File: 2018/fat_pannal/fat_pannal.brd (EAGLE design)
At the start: 160 x 130.5 mm, 31 parts, among them IC1 MEGA8-P, Q2 BUZ11BV, Q3 BUZ11BV, Q4 BUZ11BV, Q5 BUZ11BV, U1 TSR_1-2450

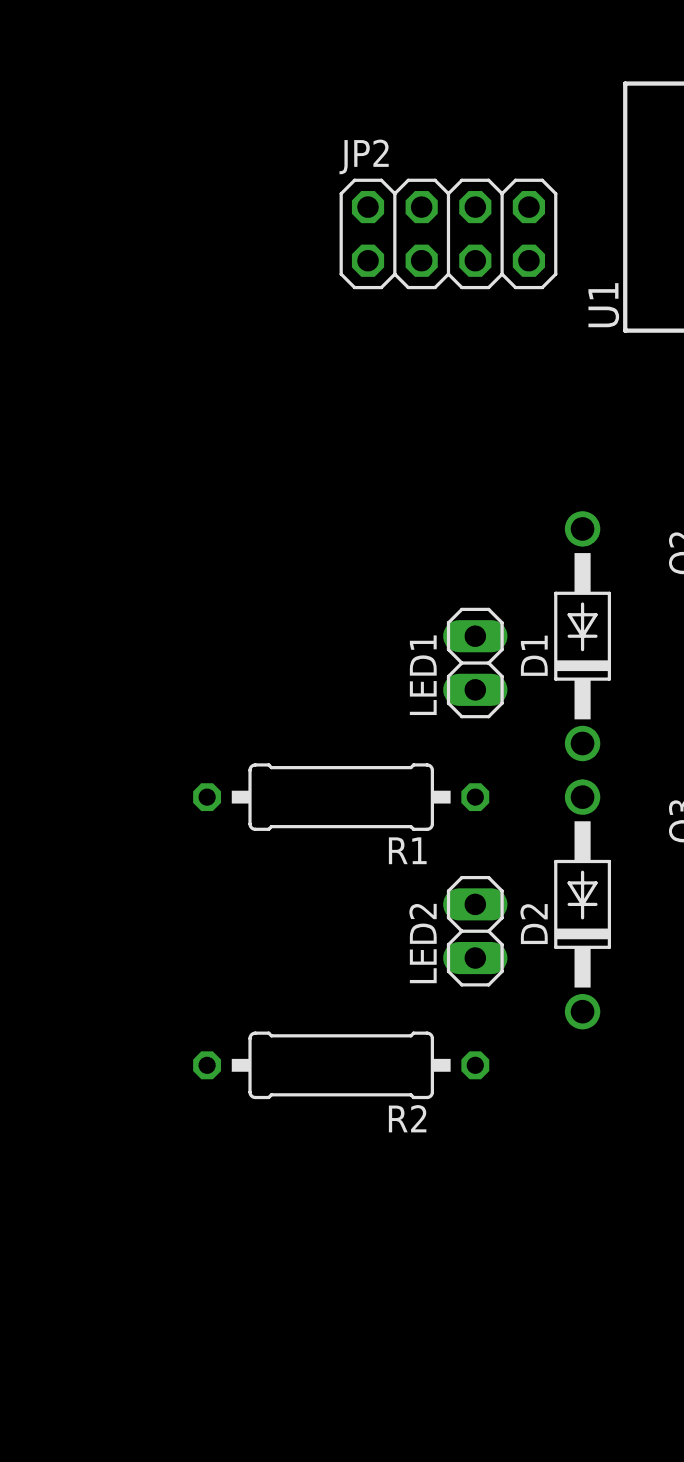
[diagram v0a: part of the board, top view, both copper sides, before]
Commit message: [FAT pannal] Split cavalier in two.
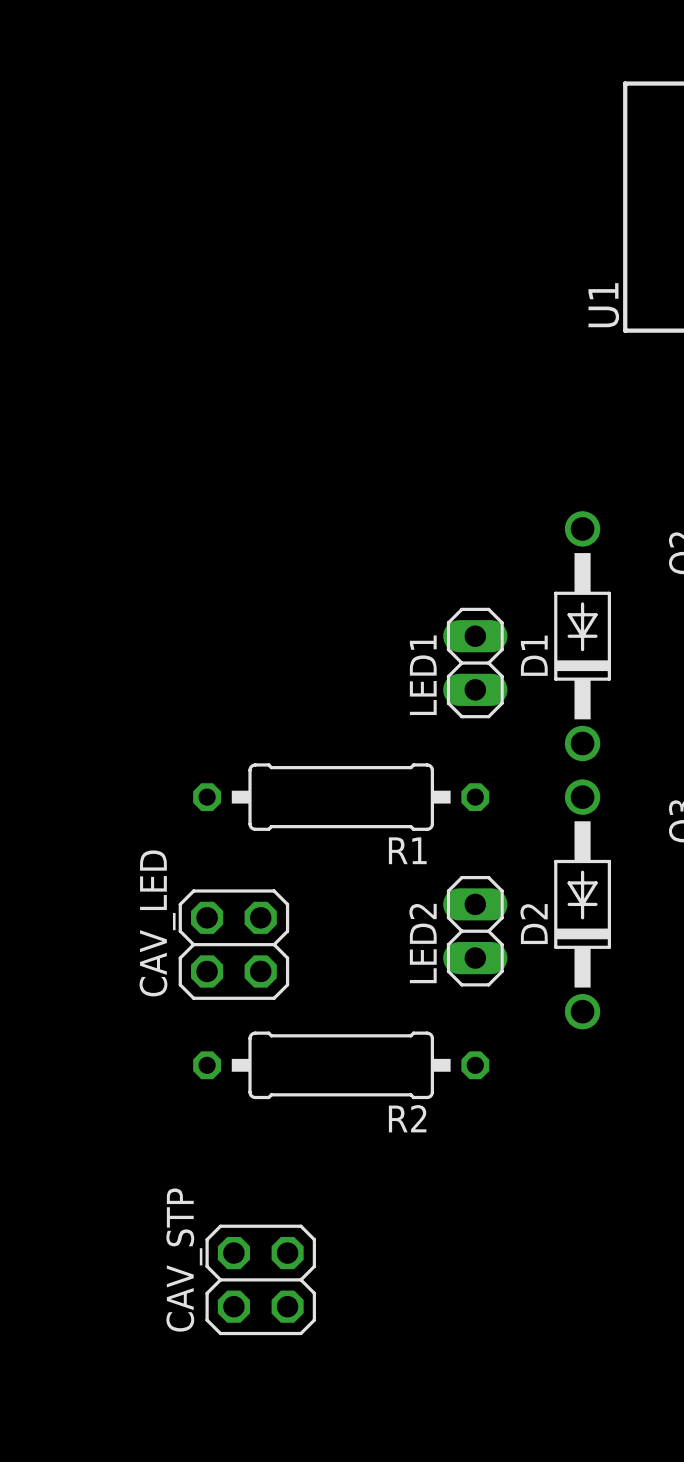
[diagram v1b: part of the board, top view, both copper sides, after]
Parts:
- removed JP2: (no value), pinhead:2X04
- added CAV_LED, CAV_STP: (no value), pinhead:2X02
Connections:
- net GND: now also CAV_LED.1, CAV_LED.3, CAV_STP.1, CAV_STP.3; no longer JP2.1, JP2.3, JP2.5, JP2.7
- net VBAT: now also CAV_LED.2, CAV_STP.2; no longer JP2.4, JP2.6
- net VLED: now also CAV_LED.4; no longer JP2.8
- net VMOT: now also CAV_STP.4; no longer JP2.2
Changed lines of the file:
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@@
 <element name="SERVO3" library="pinhead" package="1X03" value="" x="91.44" y="58.42" rot="R180"/>
 <element name="REGU_5V_POWER" library="diy-modules" package="DC-DC-STEP-DOWN-LM2596" value="DC-DC-STEP-DOWN-LM2596" x="73.66" y="85.09"/>
-<element name="JP2" library="pinhead" package="2X04" value="" x="34.29" y="57.15"/>
 <element name="I2C" library="pinhead" package="1X04" value="" x="101.6" y="62.23" rot="R90"/>
 <element name="UART" library="pinhead" package="1X04" value="" x="60.96" y="59.69" rot="R90"/>
@@
 </element>
 <element name="U1" library="_traco_tsr-1" package="TSR-1" value="TSR_1-2450" x="48.26" y="58.42" rot="R90"/>
+<element name="CAV_STP" library="pinhead" package="2X02" value="" x="25.4" y="7.62" rot="R90"/>
+<element name="CAV_LED" library="pinhead" package="2X02" value="" x="24.13" y="23.495" rot="R90"/>
 </elements>
 <signals>
@@
 <contactref element="REGU_5V_POWER" pad="OUT-"/>
 <contactref element="X1" pad="2"/>
-<contactref element="JP2" pad="1"/>
-<contactref element="JP2" pad="3"/>
-<contactref element="JP2" pad="5"/>
-<contactref element="JP2" pad="7"/>
 <contactref element="STEPPER_DRIVER" pad="GND2"/>
 <contactref element="UART" pad="2"/>
 <contactref element="I2C" pad="2"/>
 <contactref element="U1" pad="2"/>
+<contactref element="CAV_LED" pad="1"/>
+<contactref element="CAV_LED" pad="3"/>
+<contactref element="CAV_STP" pad="3"/>
+<contactref element="CAV_STP" pad="1"/>
 <wire x1="101.6" y1="60.96" x2="93.472" y2="76.454" width="0" layer="19" extent="1-1"/>
 <wire x1="93.98" y1="58.42" x2="101.6" y2="60.96" width="0" layer="19" extent="1-1"/>
@@
 <wire x1="60.96" y1="58.42" x2="58.42" y2="41.91" width="0" layer="19" extent="1-1"/>
 <wire x1="48.26" y1="58.42" x2="60.96" y2="58.42" width="0" layer="19" extent="1-1"/>
-<wire x1="38.1" y1="55.88" x2="48.26" y2="58.42" width="0" layer="19" extent="1-1"/>
-<wire x1="35.56" y1="55.88" x2="38.1" y2="55.88" width="0" layer="19" extent="1-1"/>
-<wire x1="33.02" y1="55.88" x2="35.56" y2="55.88" width="0" layer="19" extent="1-1"/>
-<wire x1="30.48" y1="55.88" x2="33.02" y2="55.88" width="0" layer="19" extent="1-1"/>
 <wire x1="53.848" y1="76.454" x2="48.26" y2="58.42" width="0" layer="19" extent="1-1"/>
 <wire x1="38.1" y1="81.3308" x2="53.848" y2="76.454" width="0" layer="19" extent="1-1"/>
 <wire x1="66.04" y1="7.62" x2="48.26" y2="22.86" width="0" layer="19" extent="1-1"/>
 <wire x1="81.28" y1="7.62" x2="66.04" y2="7.62" width="0" layer="19" extent="1-1"/>
+<wire x1="25.4" y1="24.765" x2="48.26" y2="35.56" width="0" layer="19" extent="1-1"/>
+<wire x1="25.4" y1="22.225" x2="25.4" y2="24.765" width="0" layer="19" extent="1-1"/>
+<wire x1="26.67" y1="8.89" x2="48.26" y2="22.86" width="0" layer="19" extent="1-1"/>
+<wire x1="26.67" y1="6.35" x2="26.67" y2="8.89" width="0" layer="19" extent="1-1"/>
 </signal>
 <signal name="N$3">
@@
 <contactref element="R3" pad="2"/>
 <contactref element="R4" pad="2"/>
-<contactref element="JP2" pad="8"/>
+<contactref element="CAV_LED" pad="4"/>
 <wire x1="121.92" y1="17.78" x2="121.92" y2="30.48" width="0" layer="19" extent="1-1"/>
-<wire x1="38.1" y1="58.42" x2="121.92" y2="30.48" width="0" layer="19" extent="1-1"/>
-<wire x1="22.86" y1="30.48" x2="38.1" y2="58.42" width="0" layer="19" extent="1-1"/>
+<wire x1="22.86" y1="30.48" x2="121.92" y2="30.48" width="0" layer="19" extent="1-1"/>
+<wire x1="22.86" y1="24.765" x2="22.86" y2="30.48" width="0" layer="19" extent="1-1"/>
 <wire x1="22.86" y1="17.78" x2="22.86" y2="30.48" width="0" layer="19" extent="1-1"/>
 </signal>
@@
 <contactref element="REGU_5V_POWER" pad="IN+"/>
 <contactref element="X1" pad="1"/>
-<contactref element="JP2" pad="4"/>
-<contactref element="JP2" pad="6"/>
 <contactref element="U1" pad="1"/>
+<contactref element="CAV_LED" pad="2"/>
+<contactref element="CAV_STP" pad="2"/>
 <wire x1="38.1" y1="86.3346" x2="53.848" y2="93.726" width="0" layer="19" extent="1-1"/>
-<wire x1="35.56" y1="58.42" x2="38.1" y2="86.3346" width="0" layer="19" extent="1-1"/>
-<wire x1="33.02" y1="58.42" x2="35.56" y2="58.42" width="0" layer="19" extent="1-1"/>
-<wire x1="48.26" y1="55.88" x2="35.56" y2="58.42" width="0" layer="19" extent="1-1"/>
+<wire x1="48.26" y1="55.88" x2="38.1" y2="86.3346" width="0" layer="19" extent="1-1"/>
+<wire x1="22.86" y1="22.225" x2="48.26" y2="55.88" width="0" layer="19" extent="1-1"/>
+<wire x1="24.13" y1="6.35" x2="22.86" y2="22.225" width="0" layer="19" extent="1-1"/>
 </signal>
 <signal name="VMOT">
-<contactref element="JP2" pad="2"/>
 <contactref element="STEPPER_DRIVER" pad="VMOT"/>
-<wire x1="83.82" y1="7.62" x2="30.48" y2="58.42" width="0" layer="19" extent="1-1"/>
+<contactref element="CAV_STP" pad="4"/>
+<wire x1="24.13" y1="8.89" x2="83.82" y2="7.62" width="0" layer="19" extent="1-1"/>
 </signal>
 </signals>

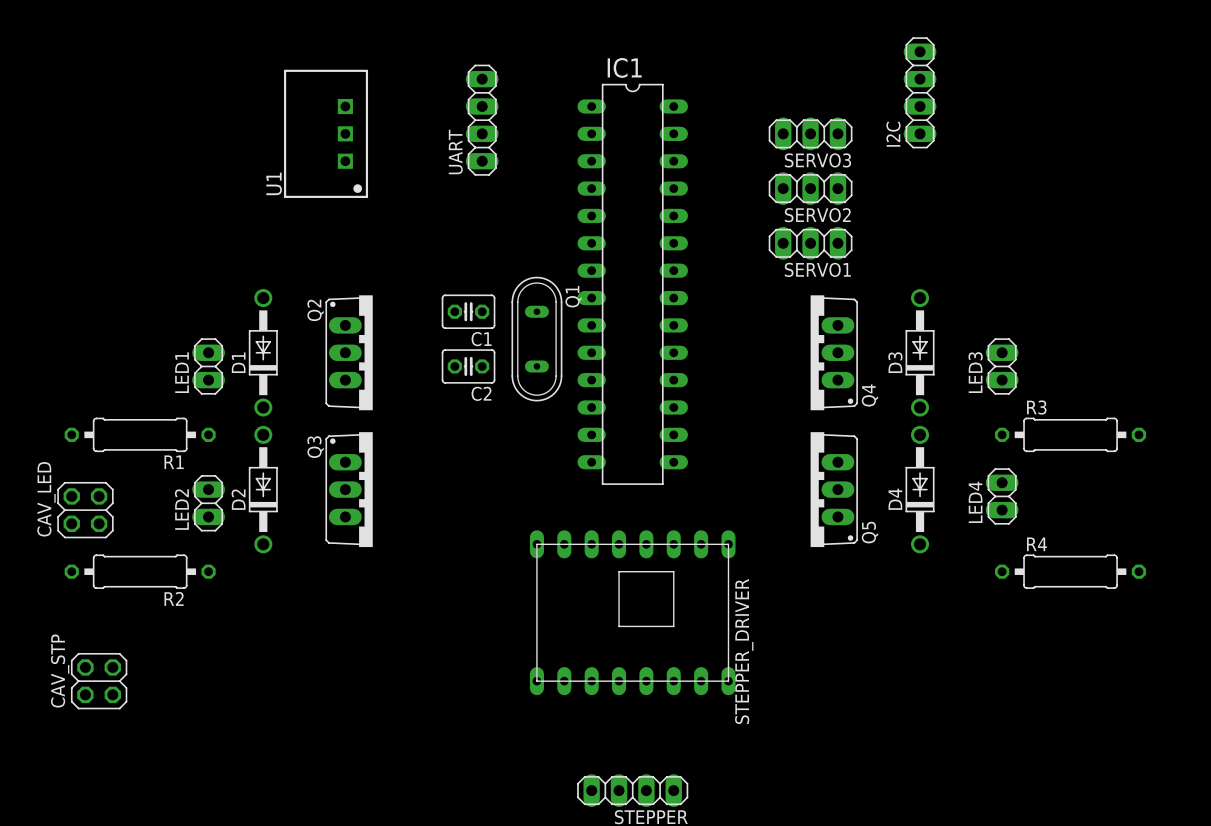
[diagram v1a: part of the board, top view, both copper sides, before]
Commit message: [FAT pannal] Begins routing.
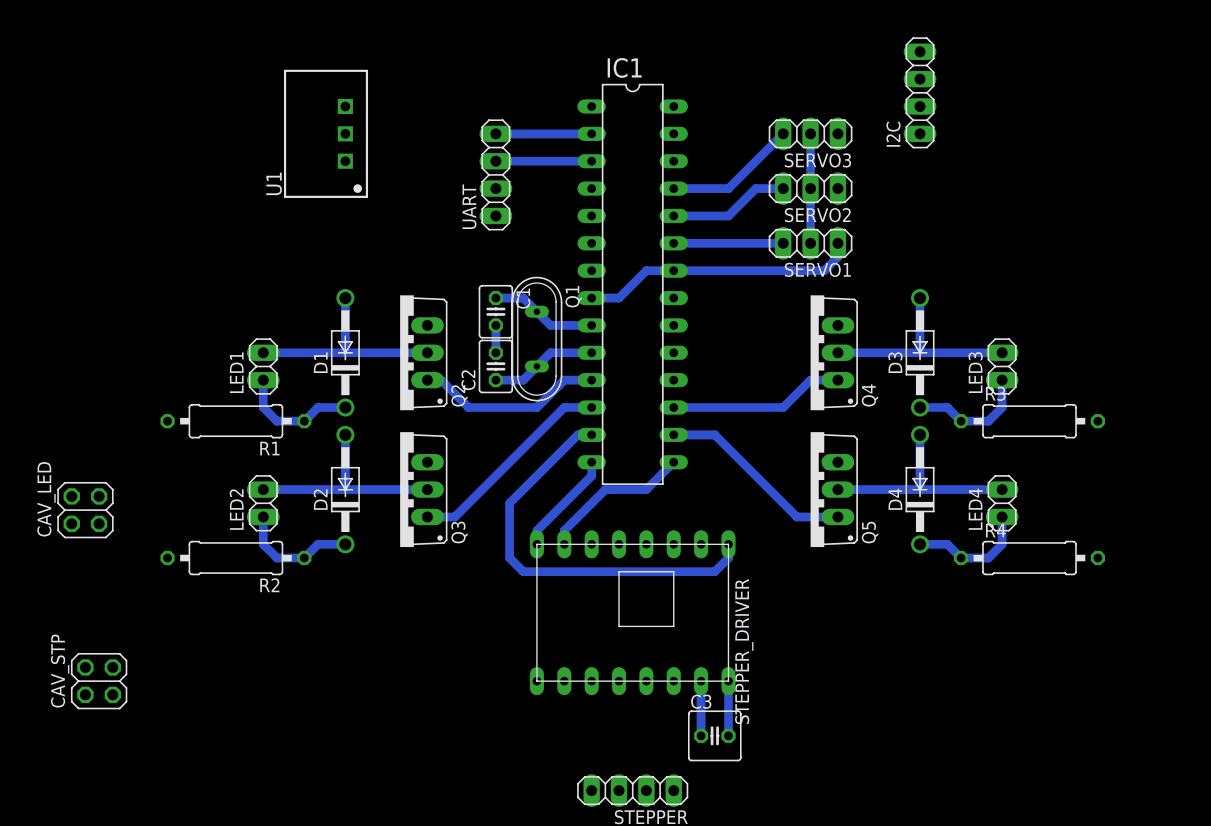
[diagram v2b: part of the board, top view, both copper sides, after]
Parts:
- added C3: 100uF, rcl:C025-050X050
- moved R1 8.98 mm to (38.1, 31.8)
- moved R2 8.98 mm to (38.1, 19.1)
- moved D1 7.62 mm to (48.3, 38.1)
- moved D2 7.62 mm to (48.3, 25.4)
- moved UART 5.24 mm to (62.2, 54.6)
- moved LED1 5.08 mm to (40.6, 36.8)
- moved LED2 5.08 mm to (40.6, 24.1)
- moved R3 4.02 mm to (111.8, 31.8)
- moved R4 4.02 mm to (111.8, 19.1)
- moved Q2 2.54 mm to (53.3, 38.1), turned to 90 degrees
- moved Q3 2.54 mm to (53.3, 25.4), turned to 90 degrees
- moved C1 2.54 mm to (62.2, 41.9), turned to 270 degrees
- moved C2 2.54 mm to (62.2, 36.8), turned to 90 degrees
- moved LED4 0.64 mm to (109.2, 24.1)
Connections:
- net GND: now also C3.1
- net VMOT: now also C3.2
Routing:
- net N$10: track 0.00 -> 38.0 mm
- net GND: track 0.00 -> 33.3 mm
- net N$27: track 0.00 -> 20.3 mm
- net N$26: track 0.00 -> 20.3 mm
- net N$29: track 0.00 -> 20.3 mm
- net N$28: track 0.00 -> 20.3 mm
- net PD6: track 0.00 -> 19.4 mm
- net PB2: track 0.00 -> 18.4 mm
- net PD5: track 0.00 -> 17.3 mm
- net PB3: track 0.00 -> 16.3 mm
- net N$2: track 0.00 -> 14.1 mm
- net SERV3: track 0.00 -> 12.3 mm
- net SERV2: track 0.00 -> 11.2 mm
- net N$23: track 0.00 -> 11.2 mm
- net N$24: track 0.00 -> 11.2 mm
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
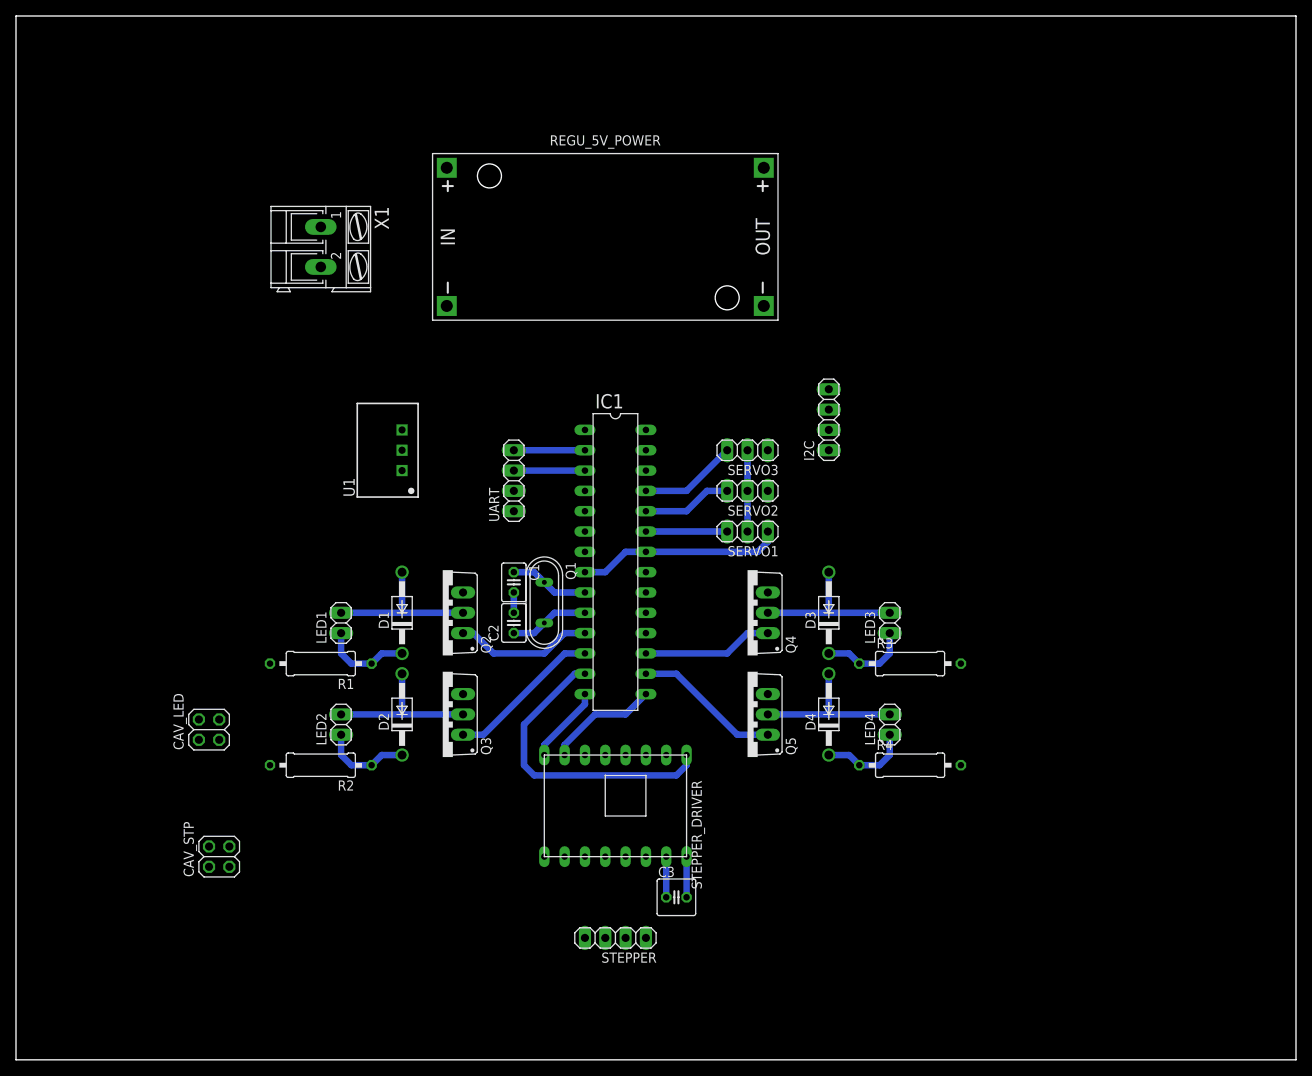
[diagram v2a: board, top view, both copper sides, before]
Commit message: [FAT pannal] Continue routing.
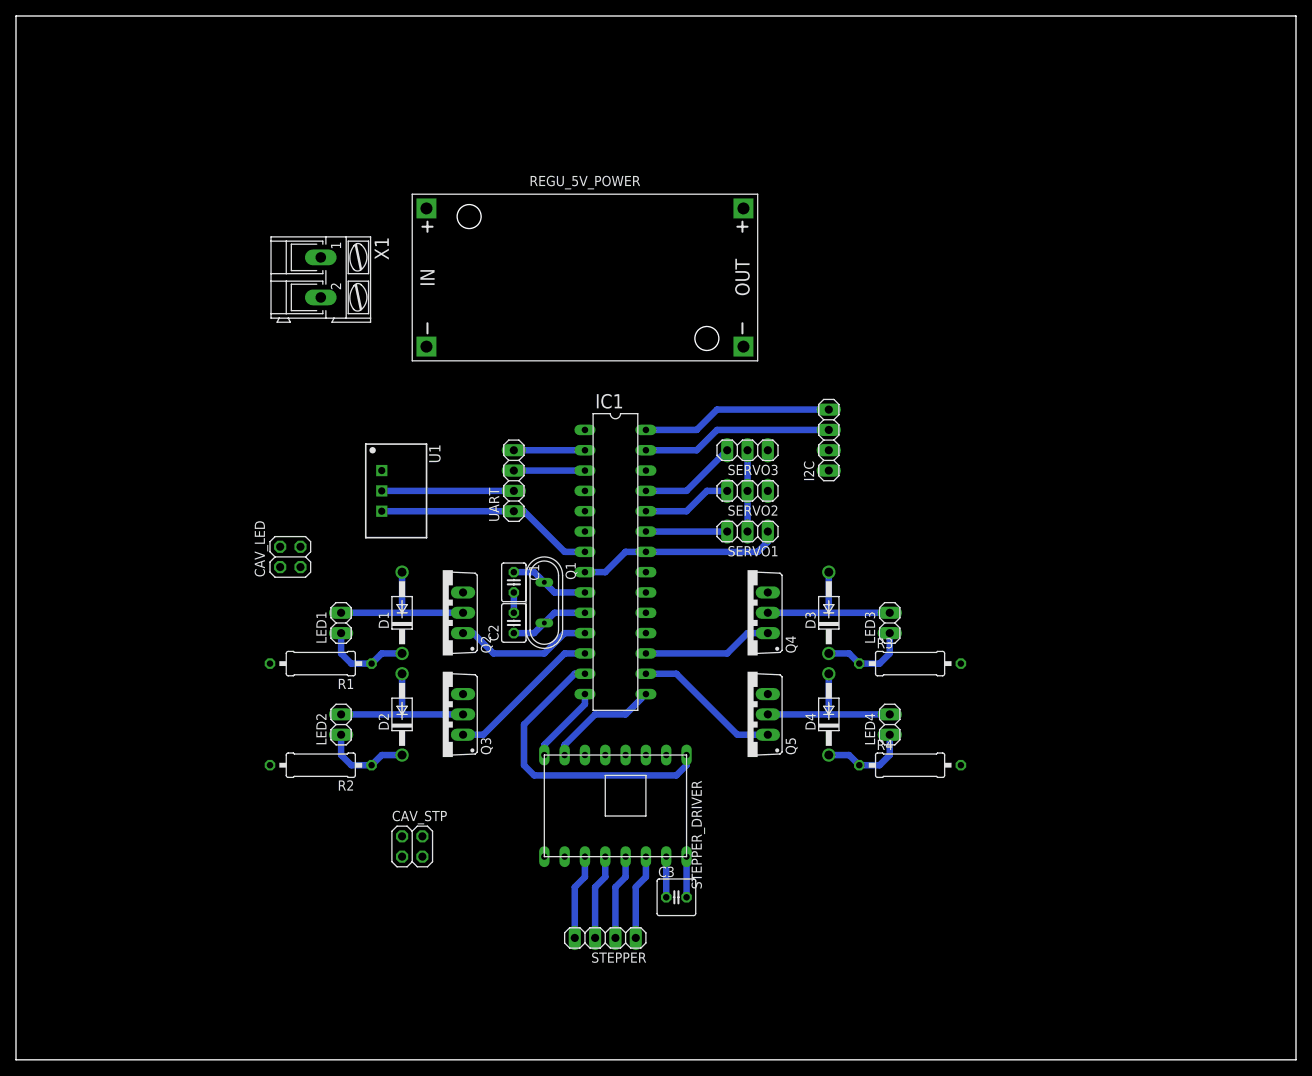
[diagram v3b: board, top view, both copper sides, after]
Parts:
- moved CAV_STP 24.2 mm to (49.5, 8.89), turned to 0 degrees
- moved CAV_LED 23.9 mm to (34.3, 45.1)
- moved U1 5.68 mm to (45.7, 53.3), turned to 270 degrees
- moved REGU_5V_POWER 5.68 mm to (71.1, 80.0)
- moved X1 3.81 mm to (38.1, 80.0)
- moved I2C 2.54 mm to (101.6, 59.7)
- moved STEPPER 1.27 mm to (73.7, -2.54)
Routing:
- net 5V_SIG: track 0.00 -> 27.5 mm
- net SDA: track 0.00 -> 23.9 mm
- net SCL: track 0.00 -> 23.9 mm
- net GND: track 33.3 -> 49.8 mm
- net N$11: track 0.00 -> 10.7 mm
- net N$14: track 0.00 -> 10.7 mm
- net N$13: track 0.00 -> 10.7 mm
- net N$12: track 0.00 -> 10.7 mm

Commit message: [FAT pannal] Finish board V1.
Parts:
- moved I2C 31.2 mm to (73.7, 73.7)
- moved R3 30.2 mm to (83.8, 43.2)
- moved R4 30.2 mm to (83.8, 30.5)
- moved CAV_STP 30.2 mm to (21.6, 20.3)
- moved IC1 30.2 mm to (47.0, 55.9)
- moved LED1 30.2 mm to (12.7, 48.3)
- moved LED2 30.2 mm to (12.7, 35.6)
- moved Q1 30.2 mm to (38.1, 50.8)
- moved Q2 30.2 mm to (25.4, 49.5)
- moved Q3 30.2 mm to (25.4, 36.8)
- moved R1 30.2 mm to (10.2, 43.2)
- moved R2 30.2 mm to (10.2, 30.5)
- moved REGU_5V_POWER 30.2 mm to (43.2, 91.4)
- moved STEPPER_DRIVER 30.2 mm to (48.3, 24.1)
- moved C1 30.2 mm to (34.3, 53.3)
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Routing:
- net GND: track 49.8 -> 363.0 mm, vias 0 -> 12
- net 5V_SIG: track 27.5 -> 181.9 mm, vias 0 -> 2
- net VLED: track 0.00 -> 150.9 mm
- net VBAT: track 0.00 -> 114.6 mm
- net VMOT: track 5.08 -> 42.7 mm
- net 5V_POWER: track 10.2 -> 44.8 mm, vias 0 -> 2
- net N$9: track 0.00 -> 2.54 mm
- net SDA: track 23.9 -> 25.0 mm
- net SCL: track 23.9 -> 25.0 mm
- added copper zone on layer 16, net GND
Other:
- board size 160 x 130.5 mm -> 94 x 106.3 mm
- board text added: "FAT Pannal"
- board text added: "Fab@ENAC - 2018"
- board text added: "régu 5V"
